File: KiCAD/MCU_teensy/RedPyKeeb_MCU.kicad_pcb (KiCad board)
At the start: 4 copper layers, 94 x 82.5 mm, 7 parts, among them J0 Conn_01x04, J1 Conn_01x36, J2 Conn_01x04, U0 Teensy4.1, U1 TXS0104ED

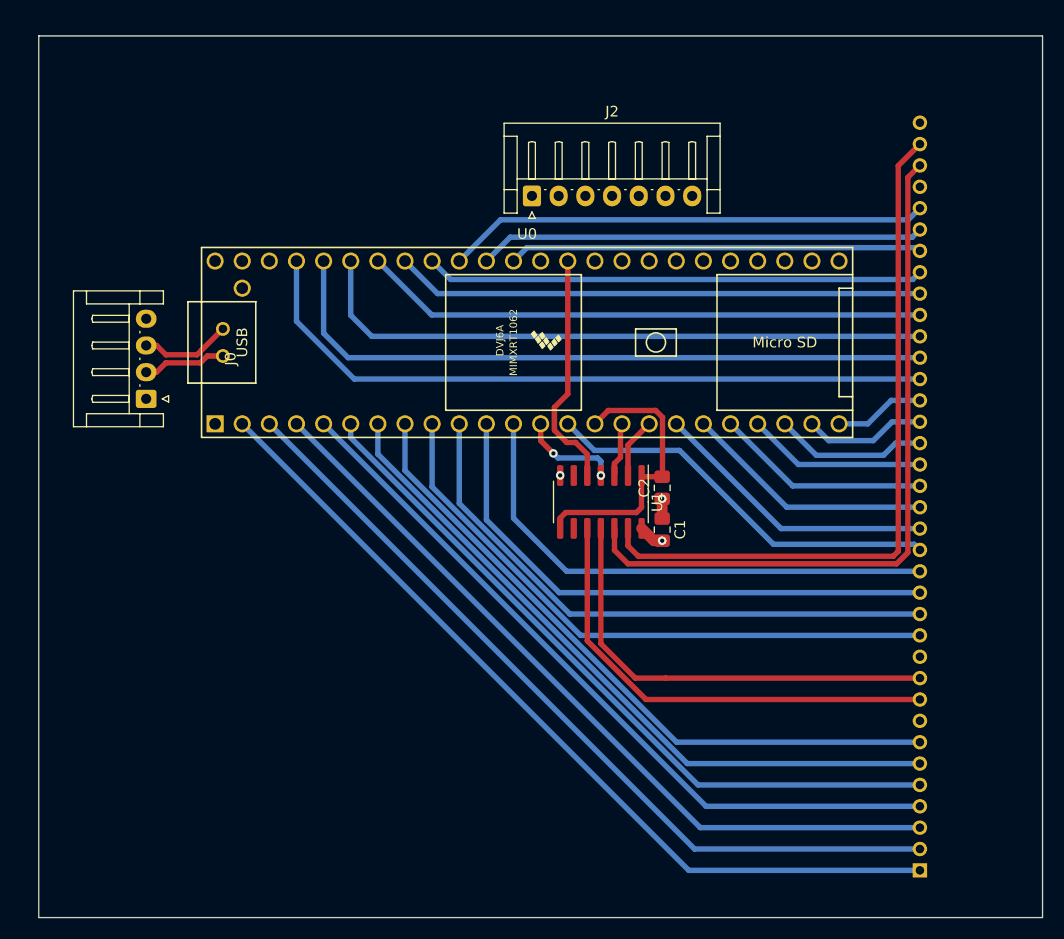
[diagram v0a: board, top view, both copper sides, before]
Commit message: Firmware is as-is for now, I've been testing PCB revisions and seeing what kind of latency I can poll the entire key matrix at KiCAD designs are looking really good now and I shoulld have parts in the next few weeks that will let me validate the keyboard as a whole plus the firmware.
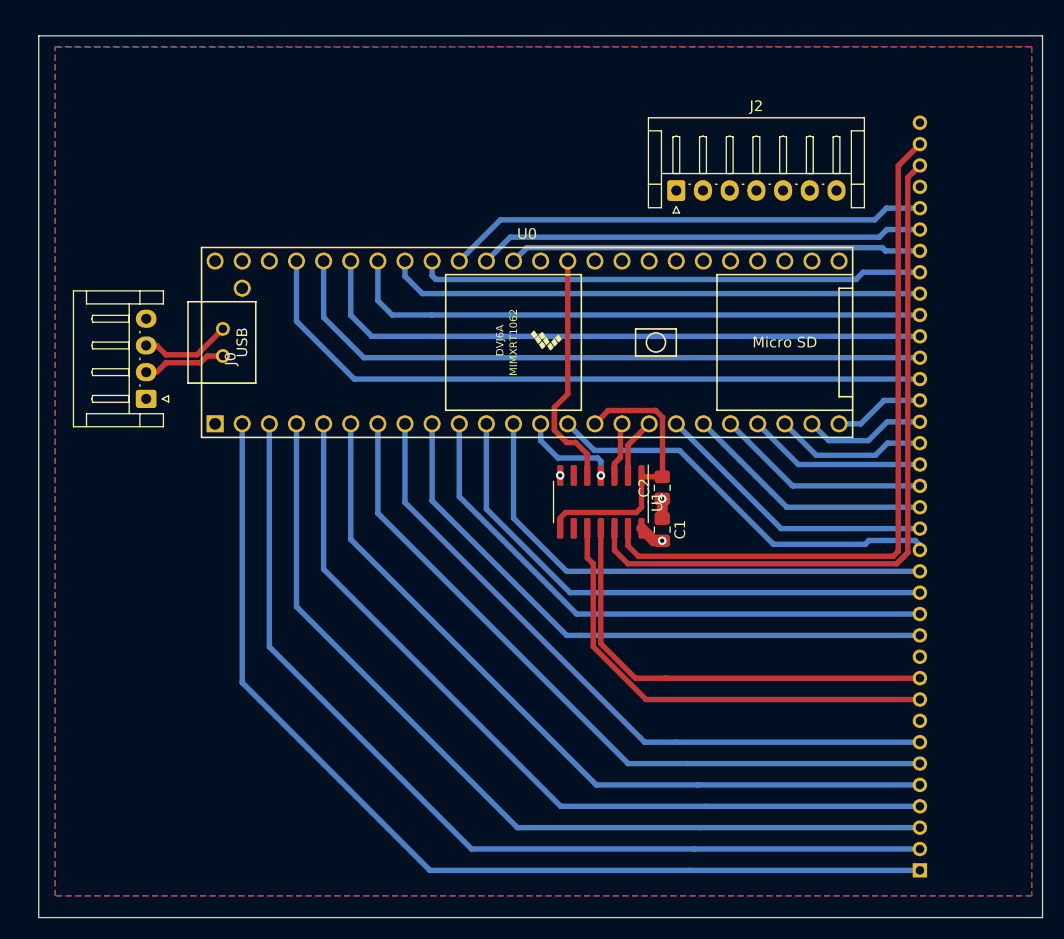
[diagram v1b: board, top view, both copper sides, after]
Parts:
- moved J2 13.5 mm to (77.5, 31.0)
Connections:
- J2 pad 1: (no net) -> MAIN_VBUS
- J2 pad 2: (no net) -> GNDPWR
- J2 pad 3: (no net) -> Net-(J2-Pad3)
- J2 pad 4: (no net) -> Net-(J2-Pad4)
- J2 pad 5: (no net) -> Net-(J2-Pad5)
- J2 pad 6: (no net) -> Net-(J2-Pad6)
- J2 pad 7: (no net) -> Net-(J2-Pad7)
- U0 pad 1: (no net) -> Net-(U0-Pad1)
- U0 pad 25: (no net) -> Net-(U0-Pad25)
- U0 pad 26: (no net) -> Net-(U0-Pad26)
- U0 pad 27: (no net) -> Net-(U0-Pad27)
- U0 pad 28: (no net) -> Net-(U0-Pad28)
- U0 pad 29: (no net) -> Net-(U0-Pad29)
- U0 pad 30: (no net) -> Net-(U0-Pad30)
- U0 pad 31: (no net) -> Net-(U0-Pad31)
- U0 pad 32: (no net) -> Net-(U0-Pad32)
- U0 pad 33: (no net) -> Net-(U0-Pad33)
- U0 pad 34: (no net) -> Net-(U0-Pad34)
- U0 pad 36: (no net) -> Net-(U0-Pad36)
- U0 pad 46: (no net) -> Net-(U0-Pad46)
- U0 pad 48: (no net) -> Net-(U0-Pad48)
- U1 pad 6: (no net) -> Net-(U1-Pad6)
- U1 pad 9: (no net) -> Net-(U1-Pad9)
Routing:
- net KEY_ROW0: track 80.8 -> 95.0 mm
- net KEY_ROW1: track 77.4 -> 89.6 mm
- net MAIN_VBUS: track 229.0 -> 241.0 mm
- net KEY_ROW2: track 74.0 -> 84.1 mm
- net GNDPWR: track 199.7 -> 209.2 mm
- net KEY_ROW3: track 70.7 -> 78.6 mm
- net KEY_ROW4: track 68.1 -> 73.6 mm
- net KEY_ROW5: track 65.6 -> 68.8 mm
- net KEY_COL15: track 52.8 -> 55.0 mm
- net KEY_ROW6: track 63.1 -> 64.9 mm
- net KEY_COL13: track 63.5 -> 62.7 mm
- net KEY_COL16: track 49.5 -> 50.3 mm
- net KEY_COL17: track 46.7 -> 47.5 mm
- net KEY_COL0: track 57.3 -> 58.1 mm
- net KEY_COL2: track 52.4 -> 51.8 mm
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- added copper zone on B.Cu, net GNDPWR
- added copper zone on F.Cu, net GNDPWR
- added copper zone on MISC, net GNDPWR

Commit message: Latest KiCAD files and what ever I had for testing the old boards.
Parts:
- added R1: ERJ-6RED2003V, Resistors_SMD:R_0805_HandSoldering, F.Cu at (63.7, 60.5)
- J1: value Conn_01x36 -> Conn_02x20_Top_Bottom; footprint Connector_PinHeader_2.00mm:PinHeader_1x36_P2.00mm_Horizontal -> Connector_PinHeader_2.54mm:PinHeader_2x20_P2.54mm_Vertical
- moved J1 19.0 mm to (100.0, 75.7)
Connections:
- J1 pad 10: LED_SDA_ROW0 -> KEY_COL2
- J1 pad 11: GNDPWR -> KEY_COL3
- J1 pad 12: KEY_COL0 -> KEY_COL4
- J1 pad 13: KEY_COL1 -> KEY_COL5
- J1 pad 14: KEY_COL2 -> KEY_COL6
- J1 pad 15: KEY_COL3 -> KEY_COL7
- J1 pad 16: KEY_COL4 -> KEY_COL8
- J1 pad 17: KEY_COL5 -> KEY_COL9
- J1 pad 18: KEY_COL6 -> KEY_COL10
- J1 pad 19: KEY_COL7 -> KEY_COL11
- J1 pad 20: KEY_COL8 -> KEY_COL12
- J1 pad 21: KEY_COL9 -> LED_SDA_ROW0
- J1 pad 22: KEY_COL10 -> LED_SCL_ROW0
- J1 pad 23: KEY_COL11 -> KEY_COL13
- J1 pad 24: KEY_COL12 -> KEY_COL14
- J1 pad 25: KEY_COL13 -> KEY_COL15
- J1 pad 26: KEY_COL14 -> KEY_COL16
- J1 pad 27: KEY_COL15 -> KEY_COL17
- J1 pad 28: KEY_COL16 -> KEY_COL18
- J1 pad 29: KEY_COL17 -> KEY_COL19
- J1 pad 30: KEY_COL18 -> KEY_COL20
- J1 pad 31: KEY_COL19 -> Net-(J1-Pad31)
- J1 pad 32: KEY_COL20 -> Net-(J1-Pad32)
- J1 pad 33: MAIN_VBUS -> Net-(J1-Pad33)
- J1 pad 34: LED_SCL_STATUS0 -> Net-(J1-Pad34)
- J1 pad 35: LED_SDA_STATUS0 -> GNDPWR
- J1 pad 8: MAIN_VBUS -> KEY_COL0
- J1 pad 9: LED_SCL_ROW0 -> KEY_COL1
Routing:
- net MAIN_VBUS: track 241.0 -> 2.41 mm
- net GNDPWR: track 209.2 -> 1.86 mm, vias 2 -> 3
- net KEY_ROW0: track 95.0 -> 80.8 mm
- net KEY_ROW2: track 84.1 -> 69.9 mm
- net KEY_ROW1: track 89.6 -> 78.3 mm
- net KEY_ROW4: track 73.6 -> 63.0 mm
- net KEY_COL18: track 38.7 -> 48.7 mm
- net KEY_ROW3: track 78.6 -> 69.5 mm
- net LED_SDA_STATUS0: track 66.5 -> 57.5 mm
- net KEY_ROW6: track 64.9 -> 58.3 mm
- net KEY_COL12: track 66.2 -> 72.2 mm
- net LED_SCL_STATUS0: track 67.2 -> 61.8 mm
- net KEY_ROW5: track 68.8 -> 63.7 mm
- net KEY_COL16: track 50.3 -> 55.2 mm
- net 33_REF: track 26.7 -> 30.7 mm
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- added copper zone on GND, net GNDPWR
- added copper zone on PWR, net MAIN_VBUS
- removed copper zone on B.Cu, net GNDPWR
- removed copper zone on F.Cu, net GNDPWR
- removed copper zone on MISC, net GNDPWR

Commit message: Minimum viable product! I still need to work out a few things on the PCBs but its finally real!
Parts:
- J1: footprint Connector_PinHeader_2.54mm:PinHeader_2x20_P2.54mm_Vertical -> Connector_PinSocket_2.54mm:PinSocket_2x20_P2.54mm_Vertical_SMD
- moved J1 24.1 mm to (101.4, 51.6)
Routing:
- net KEY_COL18: track 48.7 -> 58.0 mm
- net KEY_ROW0: track 80.8 -> 87.1 mm
- net LED_SDA_STATUS0: track 57.5 -> 63.8 mm, vias 0 -> 1
- net KEY_ROW4: track 63.0 -> 68.8 mm
- net KEY_ROW2: track 69.9 -> 75.5 mm
- net KEY_COL13: track 61.5 -> 67.1 mm
- net KEY_COL15: track 55.6 -> 61.1 mm
- net KEY_COL7: track 21.0 -> 26.6 mm
- net KEY_COL1: track 55.3 -> 60.9 mm
- net KEY_ROW6: track 58.3 -> 63.8 mm
- net KEY_COL3: track 50.1 -> 55.7 mm
- net KEY_COL5: track 27.3 -> 32.8 mm
- net KEY_COL9: track 14.3 -> 19.8 mm
- net KEY_COL11: track 7.32 -> 12.8 mm
- net KEY_COL17: track 49.4 -> 54.3 mm
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
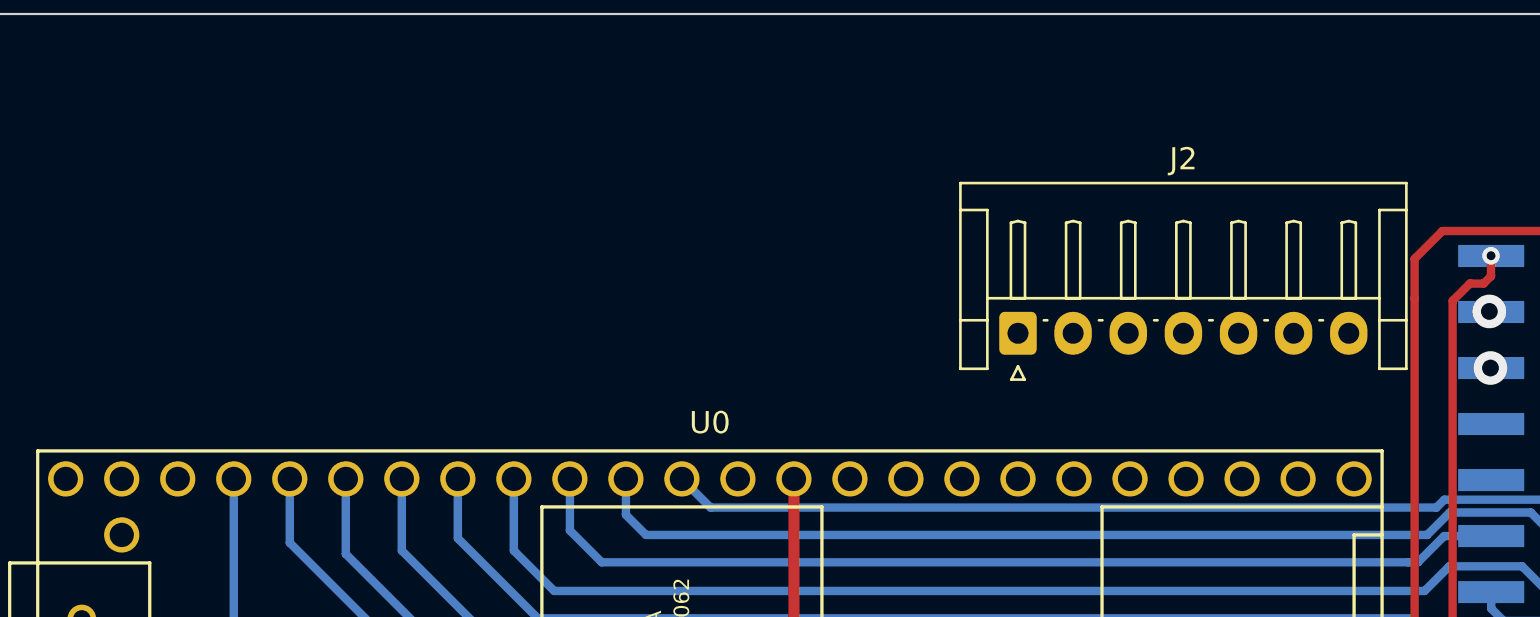
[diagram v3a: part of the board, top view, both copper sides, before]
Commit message: Add dip switch to allow for plug-in/boot time option selects. Add status light LEDs to be handled and actually reflect capslock and numlock status. Add tiny debounce which is enough on my prototype board to remove false-positive key registration on the first column.
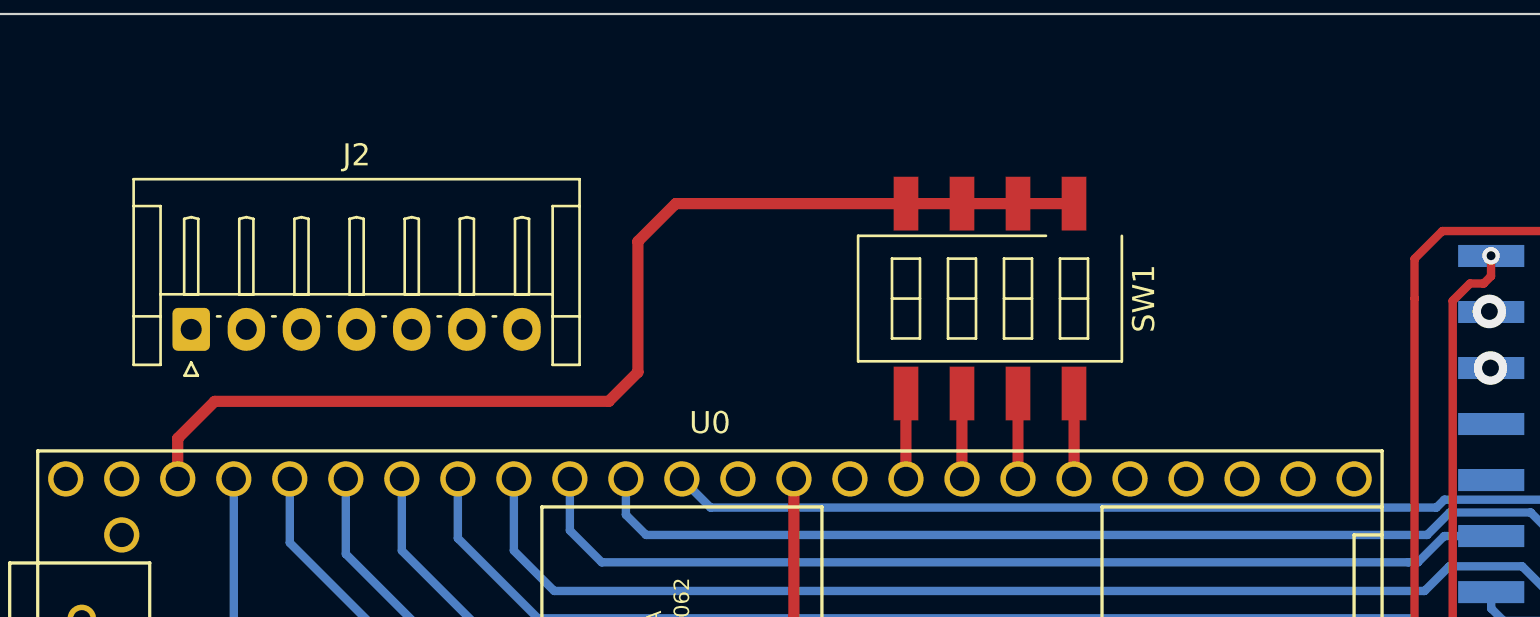
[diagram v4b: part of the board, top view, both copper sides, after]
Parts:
- added SW1: SW_DIP_x04, Buttons_Switches_SMD:SW_DIP_x4_W8.61mm_Slide_LowProfile, F.Cu at (76.2, 29.4)
- moved J2 37.5 mm to (40.0, 30.8)
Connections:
- U0 pad 46: Net-(U0-Pad46) -> 33_REF_DIP
- U0 pad 48: Net-(U0-Pad48) -> MAIN_VBUS
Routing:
- net 33_REF_DIP: track 0.00 -> 50.4 mm
- net Net-(SW1-Pad8): track 0.00 -> 3.87 mm
- net Net-(SW1-Pad7): track 0.00 -> 3.87 mm
- net Net-(SW1-Pad6): track 0.00 -> 3.87 mm
- net Net-(SW1-Pad5): track 0.00 -> 3.87 mm

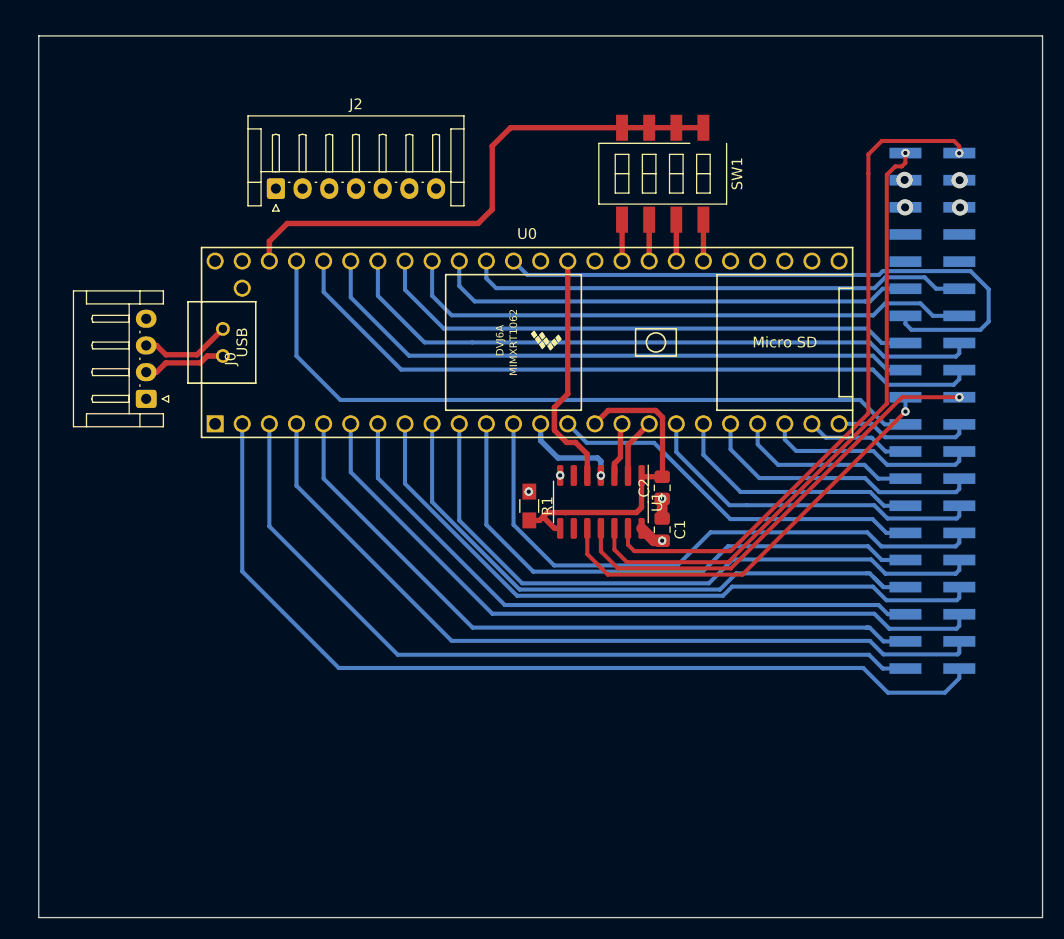
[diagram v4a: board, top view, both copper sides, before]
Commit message: Fix issues found with MCU and mainboard PCBs. Adding whatever fiddling I had with firmware.
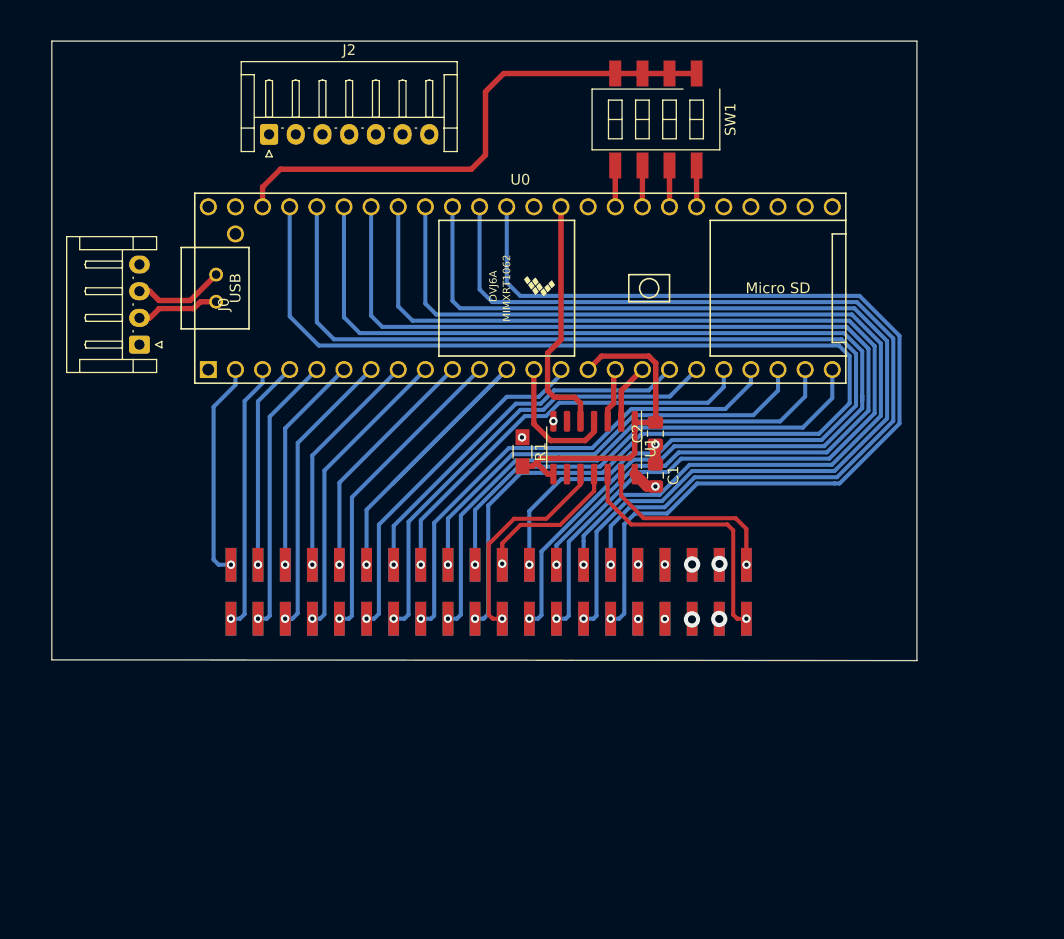
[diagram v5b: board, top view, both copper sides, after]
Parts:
- J1: footprint Connector_PinSocket_2.54mm:PinSocket_2x20_P2.54mm_Vertical_SMD -> Custom_pico:PinHeader_2x20_P2.54mm_Vertical_SMD_doublesided
- moved J1 44.9 mm to (59.9, 68.5), turned to 270 degrees
- moved U0 5.12 mm to (62.9, 40.1)
- moved R1 5.12 mm to (63.1, 55.4)
- moved SW1 5.12 mm to (75.6, 24.3)
- moved U1 5.12 mm to (69.8, 55.1)
- moved J0 5.12 mm to (27.2, 45.4)
- moved J2 5.12 mm to (39.3, 25.7)
- moved C1 5.12 mm to (75.5, 57.7)
- moved C2 5.12 mm to (75.5, 53.7)
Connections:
- U0 pad 37: KEY_COL18 -> KEY_COL20
- U0 pad 39: KEY_COL20 -> KEY_COL18
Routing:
- net KEY_ROW0: track 87.1 -> 20.5 mm, vias 0 -> 1
- net KEY_ROW2: track 75.5 -> 19.5 mm, vias 0 -> 1
- net KEY_COL16: track 51.6 -> 103.6 mm, vias 0 -> 1
- net KEY_COL14: track 58.2 -> 108.8 mm, vias 0 -> 1
- net KEY_ROW1: track 74.7 -> 25.1 mm, vias 0 -> 1
- net KEY_COL12: track 68.6 -> 118.0 mm, vias 0 -> 1
- net KEY_COL20: track 45.2 -> 93.6 mm, vias 0 -> 1
- net KEY_ROW4: track 68.8 -> 20.6 mm, vias 0 -> 1
- net LED_SDA_STATUS0: track 63.8 -> 18.4 mm
- net KEY_COL19: track 47.1 -> 90.2 mm, vias 0 -> 1
- net KEY_ROW6: track 63.8 -> 21.6 mm, vias 0 -> 1
- net KEY_COL18: track 58.0 -> 99.1 mm, vias 0 -> 1
- net KEY_COL17: track 54.3 -> 95.2 mm, vias 0 -> 1
- net KEY_COL10: track 9.83 -> 50.0 mm, vias 0 -> 1
- net KEY_COL13: track 67.1 -> 107.1 mm, vias 0 -> 1
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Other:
- board size 94 x 82.5 mm -> 81 x 58 mm
